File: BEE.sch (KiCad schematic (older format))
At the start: 54 parts, among them J1 RPI1_header, J10 Conn_01x02, J11 Conn_01x02, J12 Conn_01x02, J13 Conn_01x06, J14 Conn_01x03, J15 Conn_01x03, J16 Conn_01x08, J17 Conn_01x03, J18 Conn_01x03, J2 Conn_02x05_Odd_Even, J3 Conn_02x03_Odd_Even, J4 Conn_01x06, J5 Conn_02x10_Odd_Even, J7 Conn_02x08_Odd_Even, J8 Conn_02x08_Top_Bottom, J9 Conn_01x02, SW1 SW_Push, SW2 SW_Push, SW3 SW_Push, U1 MCP3008, U2 MCP4911

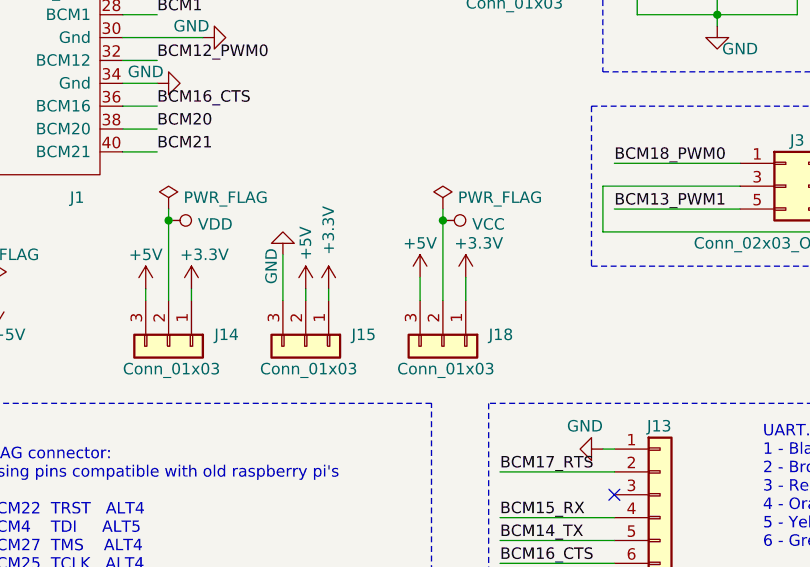
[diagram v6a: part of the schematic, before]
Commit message: Remove connector with gnd, +3.3v and +5V, and reroute
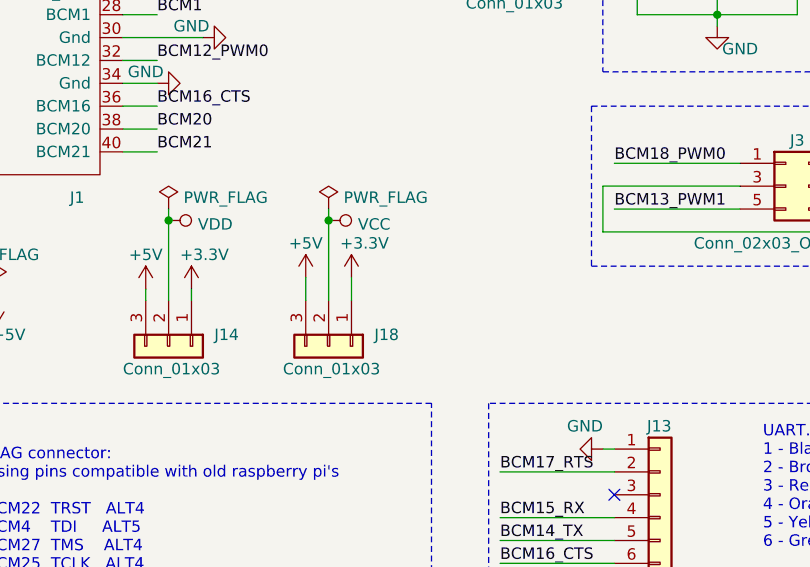
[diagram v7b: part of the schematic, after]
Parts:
- removed J15: Conn_01x03, Connector_PinHeader_2.54mm:PinHeader_1x03_P2.54mm_Vertical, symbol Connector_Generic:Conn_01x03
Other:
- moved on the sheet: J18
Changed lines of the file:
@@
 $EndComp
-$Comp
-L power:+5V #PWR021
-U 1 1 5DDBF540
-P 3600 3450
-F 0 "#PWR021" H 3600 3300 50  0001 C CNN
-F 1 "+5V" V 3600 3650 50  0000 C CNN
-F 2 "" H 3600 3450 50  0001 C CNN
-F 3 "" H 3600 3450 50  0001 C CNN
-	1    3600 3450
-	1    0    0    -1
-$EndComp
-$Comp
-L power:+3.3V #PWR018
-U 1 1 5DDBF5F5
-P 3700 3450
-F 0 "#PWR018" H 3700 3300 50  0001 C CNN
-F 1 "+3.3V" V 3700 3600 50  0000 L CNN
-F 2 "" H 3700 3450 50  0001 C CNN
-F 3 "" H 3700 3450 50  0001 C CNN
-	1    3700 3450
-	1    0    0    -1
-$EndComp
-Wire Wire Line
-	3600 3450 3600 3500
-Wire Wire Line
-	3700 3450 3700 3500
 $Comp
 L Connector_Generic:Conn_02x05_Odd_Even J2
@@
 	1    0    0    -1
 $EndComp
-$Comp
-L power:GND #PWR022
-U 1 1 5DB334E2
-P 3500 3300
-F 0 "#PWR022" H 3500 3050 50  0001 C CNN
-F 1 "GND" V 3450 3350 50  0000 C CNN
-F 2 "" H 3500 3300 50  0001 C CNN
-F 3 "" H 3500 3300 50  0001 C CNN
-	1    3500 3300
-	1    0    0    1
-$EndComp
-Wire Wire Line
-	3500 3300 3500 3500
 Connection ~ 3000 3150
 Wire Wire Line
@@
 	1    4450 2000
 	1    0    0    -1
-$EndComp
-$Comp
-L Connector_Generic:Conn_01x03 J15
-U 1 1 5DC6DC3F
-P 3600 3700
-F 0 "J15" V 3550 3900 50  0000 L CNN
-F 1 "Conn_01x03" V 3700 3500 50  0000 L CNN
-F 2 "Connector_PinHeader_2.54mm:PinHeader_1x03_P2.54mm_Vertical" H 3600 3700 50  0001 C CNN
-F 3 "https://www.mouser.es/datasheet/2/18/68000-1266375.pdf" H 3600 3700 50  0001 C CNN
-F 4 "Mouser" H -250 0   50  0001 C CNN "Distributor"
-F 5 "649-68001-403HLF" H -250 0   50  0001 C CNN "Distributor PN"
-F 6 "https://www.mouser.es/ProductDetail/Amphenol-FCI/68001-403HLF?qs=sGAEpiMZZMs%252BGHln7q6pm%2FK1Y9dcUIE1Zb6%2FMRCtGFY%3D" H -250 0   50  0001 C CNN "Distributor link"
-F 7 "Amphenol FCI" H -250 0   50  0001 C CNN "Manufacturer"
-F 8 "68001-403HLF" H -250 0   50  0001 C CNN "Manufacturer PN"
-	1    3600 3700
-	0    1    1    0
 $EndComp
 $Comp
@@
 L Connector_Generic:Conn_01x03 J18
 U 1 1 5EB17189
-P 4200 3700
-F 0 "J18" V 4150 3900 50  0000 L CNN
-F 1 "Conn_01x03" V 4300 3500 50  0000 L CNN
-F 2 "Connector_PinHeader_2.54mm:PinHeader_1x03_P2.54mm_Vertical" H 4200 3700 50  0001 C CNN
-F 3 "https://www.mouser.es/datasheet/2/18/68000-1266375.pdf" H 4200 3700 50  0001 C CNN
-F 4 "Mouser" H 1200 0   50  0001 C CNN "Distributor"
-F 5 "649-68001-403HLF" H 1200 0   50  0001 C CNN "Distributor PN"
-F 6 "https://www.mouser.es/ProductDetail/Amphenol-FCI/68001-403HLF?qs=sGAEpiMZZMs%252BGHln7q6pm%2FK1Y9dcUIE1Zb6%2FMRCtGFY%3D" H 1200 0   50  0001 C CNN "Distributor link"
-F 7 "Amphenol FCI" H 1200 0   50  0001 C CNN "Manufacturer"
-F 8 "68001-403HLF" H 1200 0   50  0001 C CNN "Manufacturer PN"
-	1    4200 3700
+P 3700 3700
+F 0 "J18" V 3650 3900 50  0000 L CNN
+F 1 "Conn_01x03" V 3800 3500 50  0000 L CNN
+F 2 "Connector_PinHeader_2.54mm:PinHeader_1x03_P2.54mm_Vertical" H 3700 3700 50  0001 C CNN
+F 3 "https://www.mouser.es/datasheet/2/18/68000-1266375.pdf" H 3700 3700 50  0001 C CNN
+F 4 "Mouser" H 700 0   50  0001 C CNN "Distributor"
+F 5 "649-68001-403HLF" H 700 0   50  0001 C CNN "Distributor PN"
+F 6 "https://www.mouser.es/ProductDetail/Amphenol-FCI/68001-403HLF?qs=sGAEpiMZZMs%252BGHln7q6pm%2FK1Y9dcUIE1Zb6%2FMRCtGFY%3D" H 700 0   50  0001 C CNN "Distributor link"
+F 7 "Amphenol FCI" H 700 0   50  0001 C CNN "Manufacturer"
+F 8 "68001-403HLF" H 700 0   50  0001 C CNN "Manufacturer PN"
+	1    3700 3700
 	0    1    1    0
 $EndComp
@@
 L power:+3.3V #PWR035
 U 1 1 5EB17236
-P 4300 3400
-F 0 "#PWR035" H 4300 3250 50  0001 C CNN
-F 1 "+3.3V" H 4250 3550 50  0000 L CNN
-F 2 "" H 4300 3400 50  0001 C CNN
-F 3 "" H 4300 3400 50  0001 C CNN
-	1    4300 3400
+P 3800 3400
+F 0 "#PWR035" H 3800 3250 50  0001 C CNN
+F 1 "+3.3V" H 3750 3550 50  0000 L CNN
+F 2 "" H 3800 3400 50  0001 C CNN
+F 3 "" H 3800 3400 50  0001 C CNN
+	1    3800 3400
 	1    0    0    -1
 $EndComp
@@
 L power:+5V #PWR033
 U 1 1 5EB172B1
-P 4100 3400
-F 0 "#PWR033" H 4100 3250 50  0001 C CNN
-F 1 "+5V" H 4100 3550 50  0000 C CNN
-F 2 "" H 4100 3400 50  0001 C CNN
-F 3 "" H 4100 3400 50  0001 C CNN
-	1    4100 3400
+P 3600 3400
+F 0 "#PWR033" H 3600 3250 50  0001 C CNN
+F 1 "+5V" H 3600 3550 50  0000 C CNN
+F 2 "" H 3600 3400 50  0001 C CNN
+F 3 "" H 3600 3400 50  0001 C CNN
+	1    3600 3400
 	1    0    0    -1
 $EndComp
@@
 L power:PWR_FLAG #FLG04
 U 1 1 5EB1732C
-P 4200 3100
-F 0 "#FLG04" H 4200 3175 50  0001 C CNN
-F 1 "PWR_FLAG" H 4450 3150 50  0000 C CNN
-F 2 "" H 4200 3100 50  0001 C CNN
-F 3 "~" H 4200 3100 50  0001 C CNN
-	1    4200 3100
-	1    0    0    -1
-$EndComp
-Wire Wire Line
-	4100 3400 4100 3500
-Wire Wire Line
-	4200 3100 4200 3150
-Wire Wire Line
-	4300 3400 4300 3500
+P 3700 3100
+F 0 "#FLG04" H 3700 3175 50  0001 C CNN
+F 1 "PWR_FLAG" H 3950 3150 50  0000 C CNN
+F 2 "" H 3700 3100 50  0001 C CNN
+F 3 "~" H 3700 3100 50  0001 C CNN
+	1    3700 3100
+	1    0    0    -1
+$EndComp
+Wire Wire Line
+	3600 3400 3600 3500
+Wire Wire Line
+	3700 3100 3700 3150
+Wire Wire Line
+	3800 3400 3800 3500
 $Comp
 L power:VCC #PWR034
 U 1 1 5EB6A1D9
-P 4200 3150
-F 0 "#PWR034" H 4200 3000 50  0001 C CNN
-F 1 "VCC" V 4217 3278 50  0000 L CNN
-F 2 "" H 4200 3150 50  0001 C CNN
-F 3 "" H 4200 3150 50  0001 C CNN
-	1    4200 3150
-	0    1    1    0
-$EndComp
-Connection ~ 4200 3150
-Wire Wire Line
-	4200 3150 4200 3500
+P 3700 3150
+F 0 "#PWR034" H 3700 3000 50  0001 C CNN
+F 1 "VCC" V 3717 3278 50  0000 L CNN
+F 2 "" H 3700 3150 50  0001 C CNN
+F 3 "" H 3700 3150 50  0001 C CNN
+	1    3700 3150
+	0    1    1    0
+$EndComp
+Connection ~ 3700 3150
+Wire Wire Line
+	3700 3150 3700 3500
 $Comp
 L power:VCC #PWR036

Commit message: component changes
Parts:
- BZ1: value Buzzer -> /re
- C3: Distributor PN 581-TPSR106K006R1500 -> 581-TAJP106K006RNJ; Distributor link https://www.mouser.es/ProductDetail/AVX/TPSR106K006R1500?qs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 -> https://www.mouser.es/ProductDetail/AVX/TAJP106K006RNJ?qs=q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; Manufacturer PN TPSR106K006R1500 -> TAJP106K006RNJ
- R7: Distributor PN 603-RC0805FR-070RL -> 603-AC0805FR-070RL; Distributor link https://www.mouser.es/ProductDetail/Yageo/RC0805FR-070RL?qs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 -> https://www.mouser.es/ProductDetail/Yageo/AC0805FR-070RL?qs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; Manufacturer PN RC0805FR-070RL -> AC0805FR-070RL
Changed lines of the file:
@@
 P 6700 3100
 F 0 "BZ1" H 6853 3129 50  0000 L CNN
-F 1 "Buzzer" H 6853 3038 50  0000 L CNN
+F 1 "/re" H 6853 3038 50  0000 L CNN
 F 2 "BEElib:Buzzer" V 6675 3200 50  0001 C CNN
 F 3 "https://www.mouser.es/datasheet/2/400/iezoelectronic_buzzer_ps_en-1131915.pdf" V 6675 3200 50  0001 C CNN
@@
 F 1 "10uF" V 8200 4150 50  0000 C CNN
 F 2 "Capacitor_SMD:C_0805_2012Metric_Pad1.15x1.40mm_HandSolder" H 8288 4150 50  0001 C CNN
-F 3 "https://www.mouser.es/datasheet/2/40/tps-776850.pdf" H 8250 4300 50  0001 C CNN
+F 3 "https://www.mouser.es/datasheet/2/40/TAJ_LOW_PROFILE-932651.pdf" H 8250 4300 50  0001 C CNN
 F 4 "Mouser" H -100 850 50  0001 C CNN "Distributor"
-F 5 " 581-TPSR106K006R1500 " H -100 850 50  0001 C CNN "Distributor PN"
-F 6 "https://www.mouser.es/ProductDetail/AVX/TPSR106K006R1500?qs=sGAEpiMZZMuEN2agSAc2psKufjHBknpK0sDTr8oBm1I%3D" H -100 850 50  0001 C CNN "Distributor link"
+F 5 " 581-TAJP106K006RNJ " H -100 850 50  0001 C CNN "Distributor PN"
+F 6 "https://www.mouser.es/ProductDetail/AVX/TAJP106K006RNJ?qs=q%252BHV0zBR8MhWDNAZ3JBdYA%3D%3D" H -100 850 50  0001 C CNN "Distributor link"
 F 7 "AVX" H -100 850 50  0001 C CNN "Manufacturer"
-F 8 "TPSR106K006R1500" H -100 850 50  0001 C CNN "Manufacturer PN"
+F 8 "TAJP106K006RNJ " H -100 850 50  0001 C CNN "Manufacturer PN"
 	1    8250 4300
 	0    1    1    0
@@
 F 1 "0" V 1750 4150 50  0000 C CNN
 F 2 "Resistor_SMD:R_0805_2012Metric_Pad1.15x1.40mm_HandSolder" V 1580 4150 50  0001 C CNN
-F 3 "https://www.mouser.es/datasheet/2/447/PYu-RC_Group_51_RoHS_L_10-1527934.pdf" H 1650 4150 50  0001 C CNN
+F 3 "https://www.mouser.es/datasheet/2/447/PYu-AC_51_RoHS_L_7-1714230.pdf" H 1650 4150 50  0001 C CNN
 F 4 "Mouser" H -1050 250 50  0001 C CNN "Distributor"
-F 5 " 603-RC0805FR-070RL" H -1050 250 50  0001 C CNN "Distributor PN"
-F 6 "https://www.mouser.es/ProductDetail/Yageo/RC0805FR-070RL?qs=sGAEpiMZZMu61qfTUdNhG6gKAQVNBKOonL%252BE%2FLYSU34%3D" H -1050 250 50  0001 C CNN "Distributor link"
+F 5 " 603-AC0805FR-070RL" H -1050 250 50  0001 C CNN "Distributor PN"
+F 6 "https://www.mouser.es/ProductDetail/Yageo/AC0805FR-070RL?qs=ygRr%2FtkhteskusLKLf%2FBRw%3D%3D" H -1050 250 50  0001 C CNN "Distributor link"
 F 7 "Yageo" H -1050 250 50  0001 C CNN "Manufacturer"
-F 8 "RC0805FR-070RL" H -1050 250 50  0001 C CNN "Manufacturer PN"
+F 8 "AC0805FR-070RL" H -1050 250 50  0001 C CNN "Manufacturer PN"
 	1    1650 4150
 	0    -1   1    0
